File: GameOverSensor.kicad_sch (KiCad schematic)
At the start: 46 parts

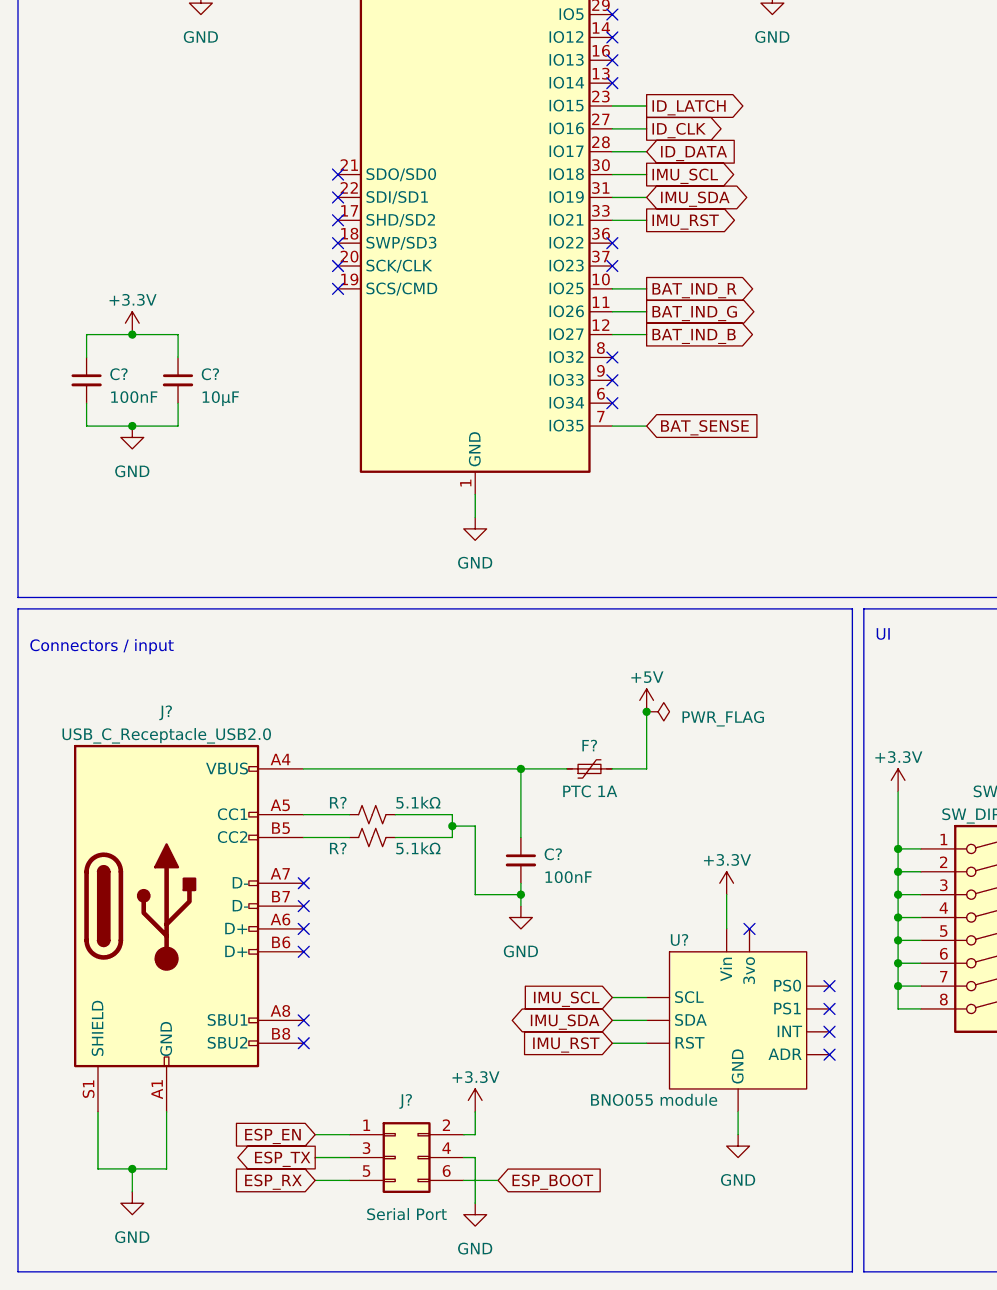
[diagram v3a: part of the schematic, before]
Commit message: Removes IMU
This PCB will be the base, on which we will connect other PCBs that add
functionality to it. The IMU will be on it's own PCB, with it's own LED.
The keypad will be a third PCB with the buttons and LEDs. The base and
the add on PCB will be connected by a FFC connector that breaks out the
the GPIO pins we're not using on the base.
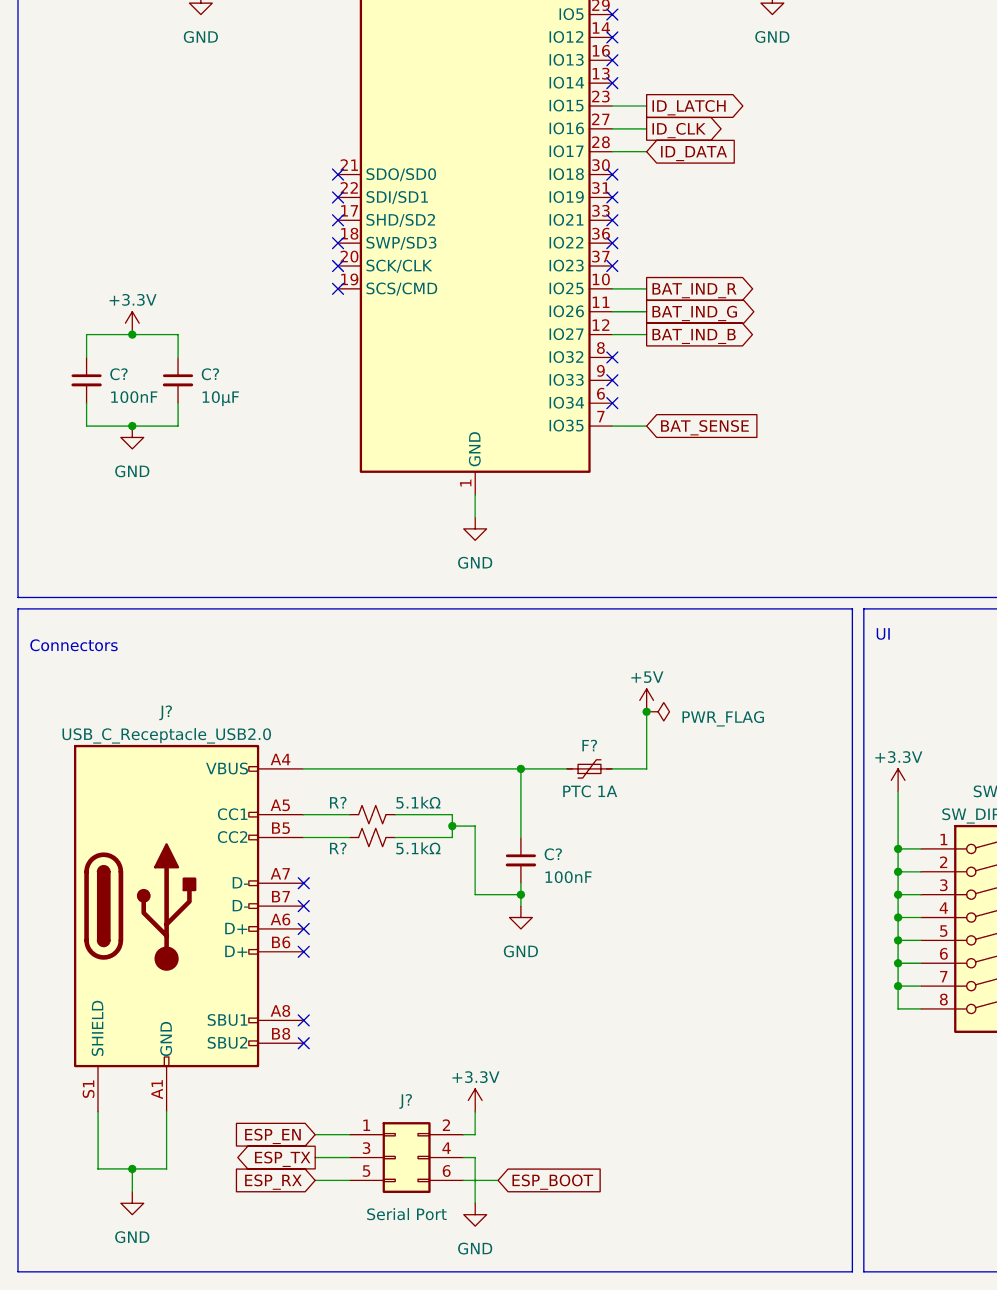
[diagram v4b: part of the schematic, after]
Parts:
- removed U?: BNO055 module, symbol GameOver:Adafruit_BNO055_breakout
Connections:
- net IMU_RST: no longer names the net of U?.33 (IO21)
- net IMU_SCL: no longer names the net of U?.30 (IO18)
- net IMU_SDA: no longer names the net of U?.31 (IO19)
- no-connect marks 32 -> 30
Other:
- note added: "Connectors"
- note removed: "Connectors / input"
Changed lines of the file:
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@@
   (no_connect (at 45.72 160.02))
   (no_connect (at 175.26 138.43))
-  (no_connect (at 104.14 166.37))
-  (no_connect (at 104.14 171.45))
-  (no_connect (at 104.14 168.91))
-  (no_connect (at 104.14 163.83))
-  (no_connect (at 95.25 157.48))
   (no_connect (at 80.01 48.26))
   (no_connect (at 80.01 55.88))
@@
   (no_connect (at 80.01 96.52))
   (no_connect (at 80.01 93.98))
+  (no_connect (at 80.01 78.74))
+  (no_connect (at 80.01 76.2))
+  (no_connect (at 80.01 73.66))
   (no_connect (at 175.26 135.89))
   (no_connect (at 45.72 170.18))
@@
     (stroke (width 0) (type default))
   )
-  (wire (pts (xy 93.98 177.8) (xy 93.98 180.34))
-    (stroke (width 0) (type default))
-  )
   (wire (pts (xy 213.36 44.45) (xy 213.36 38.1))
     (stroke (width 0) (type default))
@@
     (stroke (width 0) (type default))
   )
-  (wire (pts (xy 80.01 78.74) (xy 83.82 78.74))
-    (stroke (width 0) (type default))
-  )
   (wire (pts (xy 166.37 91.44) (xy 166.37 95.25))
     (stroke (width 0) (type default))
@@
     (stroke (width 0) (type default))
   )
-  (wire (pts (xy 80.01 170.18) (xy 83.82 170.18))
-    (stroke (width 0) (type default))
-  )
   (wire (pts (xy 114.3 148.59) (xy 111.76 148.59))
     (stroke (width 0) (type default))
@@
     (stroke (width 0) (type default))
   )
-  (wire (pts (xy 80.01 165.1) (xy 83.82 165.1))
-    (stroke (width 0) (type default))
-  )
   (wire (pts (xy 46.99 185.42) (xy 50.8 185.42))
     (stroke (width 0) (type default))
@@
     (stroke (width 0) (type default))
   )
-  (wire (pts (xy 92.71 153.67) (xy 92.71 157.48))
-    (stroke (width 0) (type default))
-  )
   (wire (pts (xy 175.26 140.97) (xy 179.07 140.97))
     (stroke (width 0) (type default))
@@
     (stroke (width 0) (type default))
   )
-  (wire (pts (xy 80.01 167.64) (xy 83.82 167.64))
-    (stroke (width 0) (type default))
-  )
   (wire (pts (xy 21.59 91.44) (xy 26.67 91.44))
     (stroke (width 0) (type default))
   )
-  (wire (pts (xy 80.01 76.2) (xy 83.82 76.2))
-    (stroke (width 0) (type default))
-  )
   (polyline (pts (xy 283.21 163.83) (xy 175.26 163.83))
     (stroke (width 0) (type default))
@@
   )
   (wire (pts (xy 187.96 93.98) (xy 187.96 92.71))
-    (stroke (width 0) (type default))
-  )
-  (wire (pts (xy 80.01 73.66) (xy 83.82 73.66))
     (stroke (width 0) (type default))
   )
@@
     (effects (font (size 1.27 1.27)) (justify left bottom))
   )
-  (text "Connectors / input" (at 15.24 127 0)
+  (text "Connectors" (at 15.24 127 0)
     (effects (font (size 1.27 1.27)) (justify left bottom))
   )
@@
     )
   )
-  (global_label "IMU_RST" (shape output) (at 83.82 78.74 0) (fields_autoplaced)
-    (effects (font (size 1.27 1.27)) (justify left))
-    (property "Intersheetrefs" "${INTERSHEET_REFS}" (id 0) (at 94.3684 78.74 0)
-      (effects (font (size 1.27 1.27)) (justify left) hide)
-    )
-  )
   (global_label "ID_CLK" (shape input) (at 152.4 135.89 180) (fields_autoplaced)
     (effects (font (size 1.27 1.27)) (justify right))
@@
     )
   )
-  (global_label "IMU_RST" (shape input) (at 80.01 170.18 180) (fields_autoplaced)
-    (effects (font (size 1.27 1.27)) (justify right))
-    (property "Intersheetrefs" "${INTERSHEET_REFS}" (id 0) (at 69.4616 170.18 0)
-      (effects (font (size 1.27 1.27)) (justify right) hide)
-    )
-  )
   (global_label "ESP_EN" (shape input) (at 29.21 43.18 180) (fields_autoplaced)
     (effects (font (size 1.27 1.27)) (justify right))
@@
     )
   )
-  (global_label "IMU_SCL" (shape input) (at 80.01 165.1 180) (fields_autoplaced)
-    (effects (font (size 1.27 1.27)) (justify right))
-    (property "Intersheetrefs" "${INTERSHEET_REFS}" (id 0) (at 69.4011 165.1 0)
-      (effects (font (size 1.27 1.27)) (justify right) hide)
-    )
-  )
   (global_label "ESP_TX" (shape output) (at 46.99 182.88 180) (fields_autoplaced)
     (effects (font (size 1.27 1.27)) (justify right))
@@
     )
   )
-  (global_label "IMU_SDA" (shape bidirectional) (at 83.82 76.2 0) (fields_autoplaced)
-    (effects (font (size 1.27 1.27)) (justify left))
-    (property "Intersheetrefs" "${INTERSHEET_REFS}" (id 0) (at 95.6007 76.2 0)
-      (effects (font (size 1.27 1.27)) (justify left) hide)
-    )
-  )
   (global_label "ID_LATCH" (shape output) (at 83.82 66.04 0) (fields_autoplaced)
     (effects (font (size 1.27 1.27)) (justify left))
@@
     )
   )
-  (global_label "IMU_SCL" (shape output) (at 83.82 73.66 0) (fields_autoplaced)
-    (effects (font (size 1.27 1.27)) (justify left))
-    (property "Intersheetrefs" "${INTERSHEET_REFS}" (id 0) (at 94.4289 73.66 0)
-      (effects (font (size 1.27 1.27)) (justify left) hide)
-    )
-  )
   (global_label "BAT_IND_G" (shape input) (at 248.92 143.51 180) (fields_autoplaced)
     (effects (font (size 1.27 1.27)) (justify right))
@@
     )
   )
-  (global_label "IMU_SDA" (shape bidirectional) (at 80.01 167.64 180) (fields_autoplaced)
-    (effects (font (size 1.27 1.27)) (justify right))
-    (property "Intersheetrefs" "${INTERSHEET_REFS}" (id 0) (at 68.2293 167.64 0)
-      (effects (font (size 1.27 1.27)) (justify right) hide)
-    )
-  )
   (global_label "ESP_BOOT" (shape input) (at 67.31 185.42 0) (fields_autoplaced)
     (effects (font (size 1.27 1.27)) (justify left))
@@
     (pin "2")
   )
-  (symbol (lib_id "power:+3.3V") (at 92.71 153.67 0) (unit 1)
-    (in_bom yes) (on_board yes) (fields_autoplaced)
-    (property "Reference" "#PWR?" (id 0) (at 92.71 157.48 0)
-      (effects (font (size 1.27 1.27)) hide)
-    )
-    (property "Value" "+3.3V" (id 1) (at 92.71 149.86 0)
-      (effects (font (size 1.27 1.27)))
-    )
-    (property "Footprint" "" (id 2) (at 92.71 153.67 0)
-      (effects (font (size 1.27 1.27)) hide)
-    )
-    (property "Datasheet" "" (id 3) (at 92.71 153.67 0)
-      (effects (font (size 1.27 1.27)) hide)
-    )
-    (pin "1")
-  )
   (symbol (lib_id "power:GND") (at 265.43 107.95 0) (unit 1)
     (in_bom yes) (on_board yes) (fields_autoplaced)
@@
     )
     (property "Datasheet" "" (id 3) (at 34.29 30.48 0)
-      (effects (font (size 1.27 1.27)) hide)
-    )
-    (pin "1")
-  )
-  (symbol (lib_id "power:GND") (at 93.98 180.34 0) (unit 1)
-    (in_bom yes) (on_board yes) (fields_autoplaced)
-    (property "Reference" "#PWR?" (id 0) (at 93.98 186.69 0)
-      (effects (font (size 1.27 1.27)) hide)
-    )
-    (property "Value" "GND" (id 1) (at 93.98 185.42 0)
-      (effects (font (size 1.27 1.27)))
-    )
-    (property "Footprint" "" (id 2) (at 93.98 180.34 0)
-      (effects (font (size 1.27 1.27)) hide)
-    )
-    (property "Datasheet" "" (id 3) (at 93.98 180.34 0)
       (effects (font (size 1.27 1.27)) hide)
     )
@@
     (pin "1")
   )
-  (symbol (lib_id "GameOver:Adafruit_BNO055_breakout") (at 93.98 167.64 0) (unit 1)
-    (in_bom yes) (on_board yes)
-    (property "Reference" "U?" (id 0) (at 86.36 158.75 0)
-      (effects (font (size 1.27 1.27)) (justify left))
-    )
-    (property "Value" "BNO055 module" (id 1) (at 77.47 176.53 0)
-      (effects (font (size 1.27 1.27)) (justify left))
-    )
-    (property "Footprint" "" (id 2) (at 93.98 167.64 0)
-      (effects (font (size 1.27 1.27)) hide)
-    )
-    (property "Datasheet" "https://learn.adafruit.com/adafruit-bno055-absolute-orientation-sensor/pinouts" (id 3) (at 93.98 167.64 0)
-      (effects (font (size 1.27 1.27)) hide)
-    )
-    (pin "")
-    (pin "")
-    (pin "")
-    (pin "")
-    (pin "")
-    (pin "")
-    (pin "")
-    (pin "")
-    (pin "")
-    (pin "")
-  )
   (symbol (lib_id "power:GND") (at 134.62 137.16 0) (unit 1)
     (in_bom yes) (on_board yes) (fields_autoplaced)
@@
       (reference "#FLG?") (unit 1) (value "PWR_FLAG") (footprint "")
     )
-    (path "/056ed8f9-9b8f-4a78-8558-d6ec70e1cd96"
-      (reference "#PWR?") (unit 1) (value "+3.3V") (footprint "")
-    )
     (path "/0735f02d-0862-4fda-ba63-78002707547b"
       (reference "#PWR?") (unit 1) (value "GND") (footprint "")
@@
       (reference "#PWR?") (unit 1) (value "+3.3V") (footprint "")
     )
-    (path "/1a587d70-a43c-41be-9338-6253db01963e"
-      (reference "#PWR?") (unit 1) (value "GND") (footprint "")
-    )
     (path "/249d46ef-861c-41d3-a19e-4af23226d63f"
       (reference "#PWR?") (unit 1) (value "GND") (footprint "")
@@
       (reference "U?") (unit 1) (value "MCP73831-2ACI-OT") (footprint "Package_TO_SOT_SMD:SOT-23-5")
     )
-    (path "/e6db6c19-49d5-4edc-94c4-41bec096b1b8"
-      (reference "U?") (unit 1) (value "BNO055 module") (footprint "")
-    )
-  )
+  )
